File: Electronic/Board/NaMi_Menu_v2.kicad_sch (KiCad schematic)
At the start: 20 parts, among them J3 Conn_01x07, J5 Conn_02x08_Odd_Even, U2 RP2305

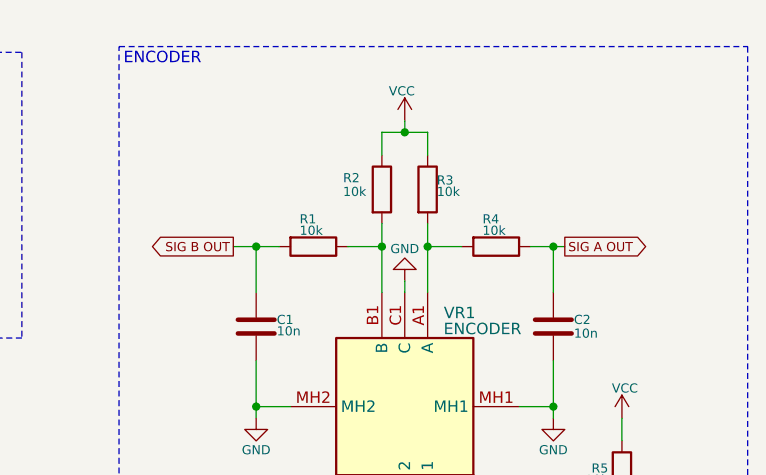
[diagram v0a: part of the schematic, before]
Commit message: Zmiana rezystorów R2 i R3 na 1k
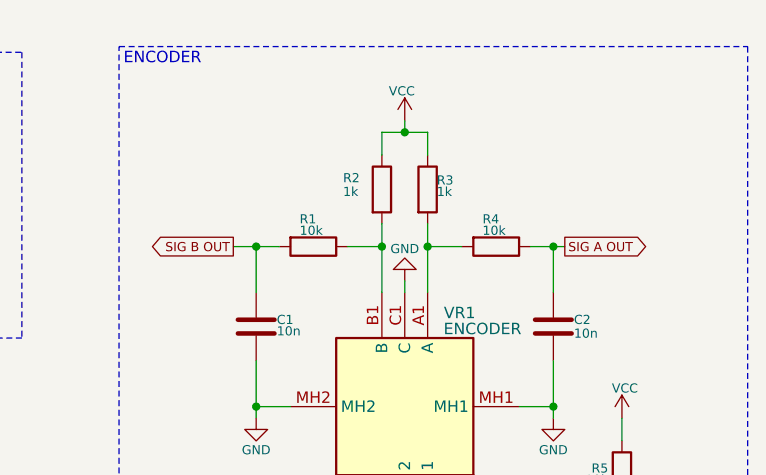
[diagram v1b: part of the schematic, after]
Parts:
- R2, R3: value 10k -> 1k
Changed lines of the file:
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@@
 			)
 		)
-		(property "Value" "10k"
+		(property "Value" "1k"
 			(at 237.236 40.894 0)
 			(effects
@@
 			)
 		)
-		(property "Value" "10k"
+		(property "Value" "1k"
 			(at 226.822 40.894 0)
 			(effects
